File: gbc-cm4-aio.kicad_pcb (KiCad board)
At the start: 4 copper layers, 70.1 x 122.2 mm, 134 parts, among them J1 Conn_01x40, J2 AudioJack2_Ground_Switch, J4 DM3D-SF, J6 Conn_01x11, J7 Conn_01x02, P1 USB_C_Plug_USB2.0, Q1 AO4407C, Q3 2N7002E, SW1 SW_Push, SW2 BOOT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

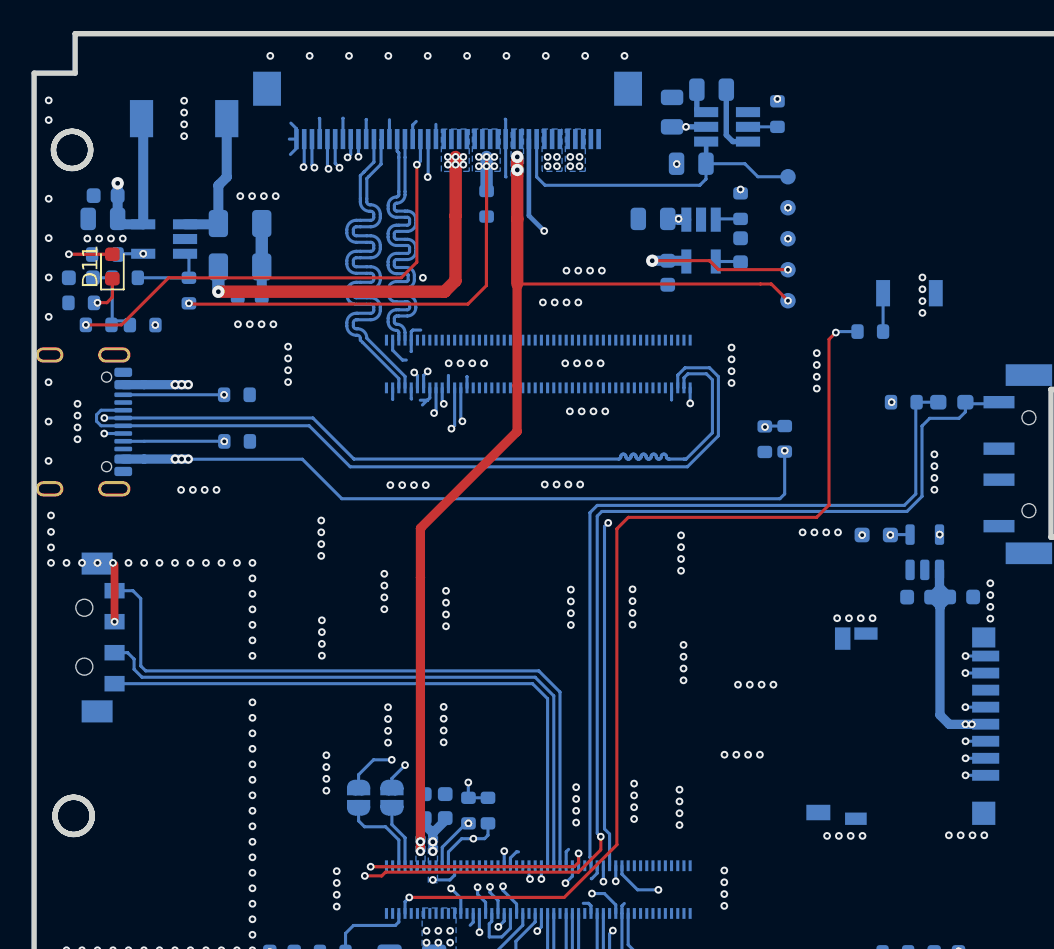
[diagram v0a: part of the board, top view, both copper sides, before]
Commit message: Backlight driver improvement
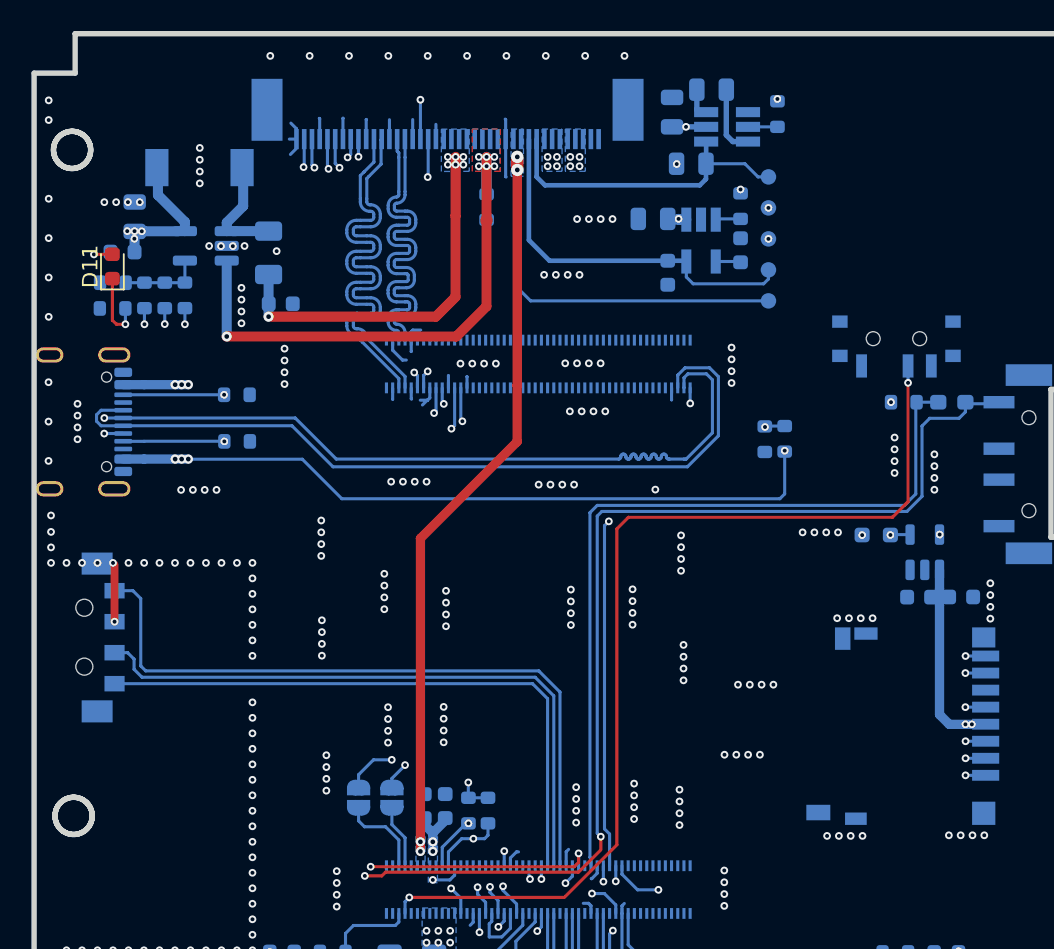
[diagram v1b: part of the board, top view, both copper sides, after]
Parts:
- removed C35: 1uF, Capacitor_SMD:C_0603_1608Metric
- removed D2: type="D" model="DIODE" lib="", Diode_SMD:D_1206_3216Metric
- removed R36: 10k, Resistor_SMD:R_0603_1608Metric
- removed R40: 220R, Resistor_SMD:R_0603_1608Metric
- removed SW2: BOOT, Button_Switch_SMD:SW_SPST_B3U-1000P
- removed U8: CAT4139, Package_TO_SOT_SMD:SOT-23-5_HandSoldering
- added SW4: SW_SPDT, Button_Switch_SMD:SW_SPDT_PCM12, B.Cu at (194.6, 155.9)
- added U2: FAN5333B, Package_TO_SOT_SMD:SOT-23-5_HandSoldering, B.Cu at (150.0, 149.5)
- C34: value 220nF -> 1uF
- L3: value 22uH -> 6.8uH
- R12: value 1k -> 10k
- moved C34 13.0 mm to (154.8, 153.3)
- moved R9 5.80 mm to (148.6, 152.7), turned to 90 degrees
- moved R12 4.94 mm to (144.0, 151.9), turned to 0 degrees
- moved R10 4.67 mm to (147.3, 152.7), turned to 90 degrees
- moved C33 3.80 mm to (144.6, 149.9)
- moved L3 3.31 mm to (149.6, 144.5)
- moved D1 2.64 mm to (154.0, 150.0), turned to 90 degrees
- moved R42 2.06 mm to (144.0, 153.6)
- moved C32 2.05 mm to (145.4, 147.7), turned to 90 degrees
- moved ? 1.78 mm to (200.8, 143.2)
- moved R11 1.69 mm to (146.0, 152.7), turned to 90 degrees
- moved +5V0 1.26 mm to (186.3, 147.1)
- moved -5V0 1.26 mm to (186.3, 145.1)
- moved 1V8 1.26 mm to (186.3, 153.1)
- moved 2V8 1.26 mm to (186.3, 151.1)
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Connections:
- C32 pad 1: +2V8 -> +3V3
- C33 pad 1: +2V8 -> +3V3
- C34 pad 1: Net-(C34-Pad1) -> GND
- C34 pad 2: GND -> /DSI1_BL_A
- D1 pad 1: Net-(D1-K) -> /DSI1_BL_A
- L3 pad 1: +2V8 -> +3V3
- R10 pad 2: Net-(C34-Pad1) -> Net-(U2-SHDN)
- R11 pad 1: Net-(C34-Pad1) -> /BL_PWM
- R11 pad 2: Net-(U8-FB) -> Net-(U2-SHDN)
- R12 pad 1: Net-(U8-FB) -> GND
- R12 pad 2: /DSI1_BL_K -> Net-(U2-SHDN)
- R9 pad 1: GND -> /BL_EN
- R9 pad 2: /BL_EN -> Net-(U2-SHDN)
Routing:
- net +2V8: track 65.1 -> 24.5 mm, vias 4 -> 0
- net /BL_EN: track 76.2 -> 67.4 mm
- net +3V3: track 30.3 -> 37.5 mm, vias 22 -> 26
- net +1V8: track 65.3 -> 71.8 mm, vias 5 -> 4
- net Net-(U2-SHDN): track 0.00 -> 5.25 mm
- net Net-(C34-Pad1): track 5.24 -> 0.00 mm
- net Net-(U8-FB): track 4.95 -> 0.00 mm
- net Net-(D1-K): track 4.70 -> 0.00 mm
- net /DSI1_BL_K: track 30.2 -> 34.0 mm
- net /DSI1_PWM: track 31.1 -> 34.0 mm
- net /DSI1_RESET: track 64.1 -> 66.6 mm
- net Net-(R40-Pad1): track 2.48 -> 0.00 mm
- net Net-(D11-K): track 2.31 -> 4.65 mm
- net Net-(D1-A): track 9.16 -> 6.84 mm
- net /BL_PWM: track 57.6 -> 59.8 mm
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- added copper zone on F.Cu, net /DSI1_BL_K
